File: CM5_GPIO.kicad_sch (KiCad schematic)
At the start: 23 parts, among them J1 Conn_02x06_Top_Bottom, J14 JST_SHBM04B-SRSS-TB, J3 Conn_01x03, J8 THD-20-R, J9 THD-02-R, SW1 Right angle Tact button, U1 TPD4EUSB30, U2 TPD4EUSB30, U3 MagJack-A70-112-331N126, U5 74LVC1G07SE-7

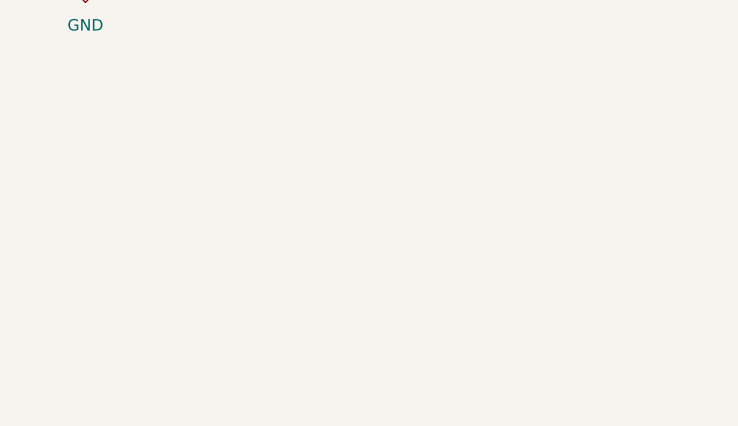
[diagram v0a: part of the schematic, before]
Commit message: Added model for Fan connector (JST_SH_BM04B-SRSS-TB_1x04-1MP_P1.00mm_Vertical) Thickened power and voltage lines Tuned all high speed lines for skew
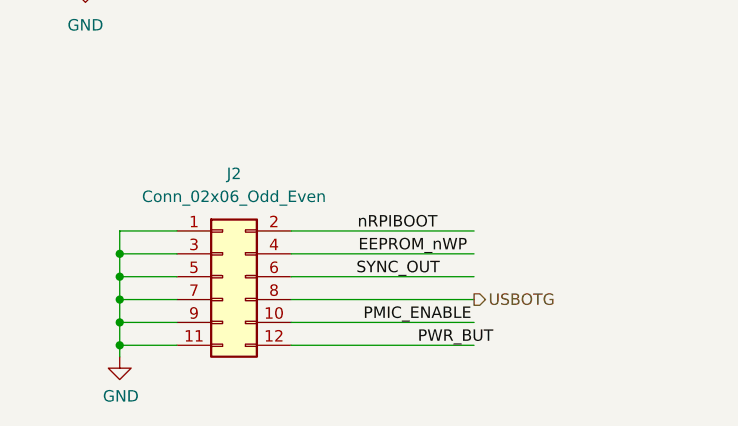
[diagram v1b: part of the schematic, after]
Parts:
- added J2: Conn_02x06_Odd_Even, Connector_PinHeader_2.54mm:PinHeader_2x06_P2.54mm_Vertical, symbol Connector_Generic:Conn_02x06_Odd_Even
- J1: footprint Connector_PinHeader_1.00mm:PinHeader_2x06_P1.00mm_Vertical -> Connector_PinHeader_2.54mm:PinHeader_2x06_P2.54mm_Vertical
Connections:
- net EEPROM_nWP: now also J2.4 (Pin_4)
- net GND: now also J2.1 (Pin_1), J2.11 (Pin_11), J2.3 (Pin_3), J2.5 (Pin_5), J2.7 (Pin_7), J2.9 (Pin_9)
- net PMIC_ENABLE: now also J2.10 (Pin_10)
- net PWR_BUT: now also J2.12 (Pin_12)
- net SYNC_OUT: now also J2.6 (Pin_6)
- net USBOTG: now also J2.8 (Pin_8)
- net nRPIBOOT: now also J2.2 (Pin_2)
